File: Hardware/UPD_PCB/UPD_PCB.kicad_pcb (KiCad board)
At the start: 6 copper layers, 145 x 65 mm, 152 parts, among them IC1 STS30-DIS, J1 25A Fuse holder, J10 796739-2, J11 Conn_01x04, J12 Conn_01x02, J2 796739-2, J3 Conn_01x02, J4 1776119-2, J5 1776119-2, J6 1776119-2, J7 1776119-2, J8 1776119-2, J9 1776119-2, Q1 LMR51635XDDCR, Q2 LMR51635XDDCR, Q3 LMR51635XDDCR, Q4 LMR51635XDDCR, Q5 LMR51635XDDCR, Q6 LMR51635XDDCR, Q7 BSS84, U1 ACS711xEXLT-31AB, U2 INA219AxD, U3 INA219AxD, U4 INA219AxD, U5 INA219AxD, U6 INA219AxD, U7 INA219AxD

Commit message: Version 1.1 of PCB
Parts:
- J12: value Conn_01x02 -> Conn_01x01; footprint Connector_PinHeader_1.00mm:PinHeader_1x02_P1.00mm_Vertical -> Connector_PinHeader_2.54mm:PinHeader_1x01_P2.54mm_Vertical
- J3: footprint Connector_PinHeader_1.00mm:PinHeader_1x02_P1.00mm_Vertical -> Connector_JST:JST_EH_B2B-EH-A_1x02_P2.50mm_Vertical
- R13, R26, R27, R36, R37: value 0.2R -> 0.1R
- R14: value 2mR -> 0.1R
- moved J3 1.08 mm to (106.5, 106.0)
- moved J12 0.96 mm to (236.6, 111.2), turned to 0 degrees
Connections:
- J12 pad 1: GND -> VIOUT
- U5 pad 1: INA_SCL -> +5V_out
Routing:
- net +5V_out: track 104.6 -> 107.2 mm
- net INA_SCL: track 200.1 -> 199.2 mm
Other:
- board text added: "5V"
- board text added: "Universal power distribution V1.1"
- board text removed: "Universal power distribution V1.0"

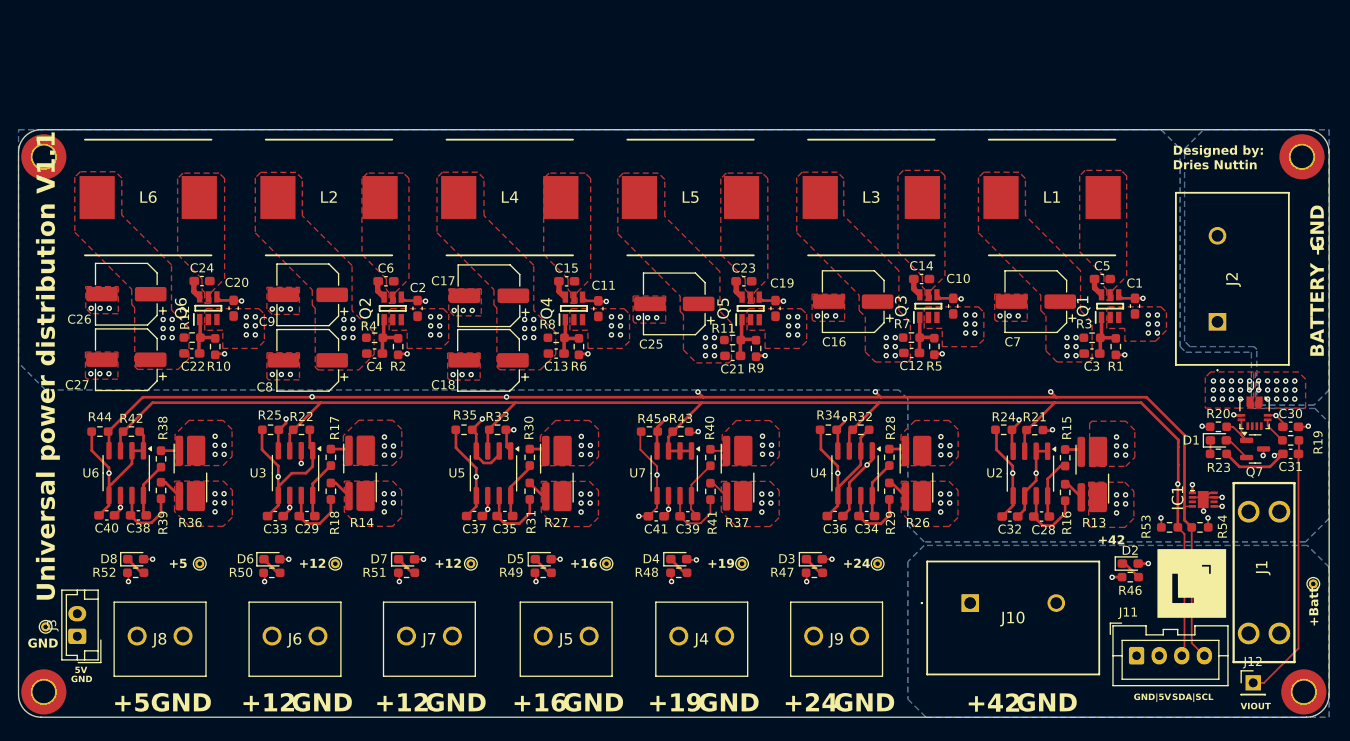
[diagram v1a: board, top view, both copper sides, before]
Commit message: Full system monitoring of PCB
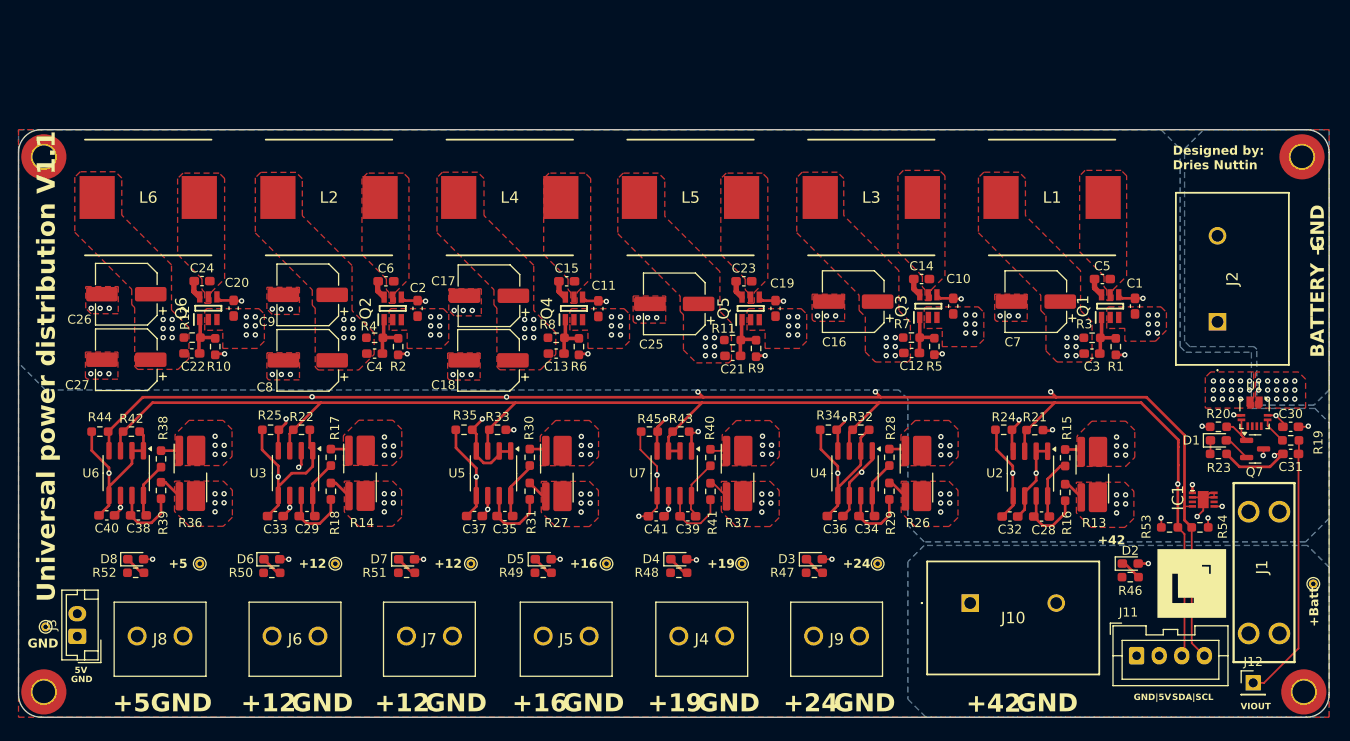
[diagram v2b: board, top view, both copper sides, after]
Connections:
- R13 pad 2: Net-(R13-Pad2) -> +24V
- R13 pad 3: Net-(R13-Pad3) -> +24V_out
- R14 pad 2: Net-(R14-Pad2) -> +12V_1
- R14 pad 3: Net-(R14-Pad3) -> +12V_1_out
- R15 pad 1: Net-(R13-Pad2) -> +24V
- R16 pad 1: Net-(R13-Pad3) -> +24V_out
- R17 pad 1: Net-(R14-Pad2) -> +12V_1
- R18 pad 1: Net-(R14-Pad3) -> +12V_1_out
- R26 pad 2: Net-(R26-Pad2) -> +19V
- R26 pad 3: Net-(R26-Pad3) -> +19V_out
- R27 pad 2: Net-(R27-Pad2) -> +12V_2
- R27 pad 3: Net-(R27-Pad3) -> +12V_2_out
- R28 pad 1: Net-(R26-Pad2) -> +19V
- R29 pad 1: Net-(R26-Pad3) -> +19V_out
- R30 pad 1: Net-(R27-Pad2) -> +12V_2
- R31 pad 1: Net-(R27-Pad3) -> +12V_2_out
- R36 pad 2: Net-(R36-Pad2) -> +5V_NS
- R36 pad 3: Net-(R36-Pad3) -> +5V_out
- R37 pad 2: Net-(R37-Pad2) -> +16V
- R37 pad 3: Net-(R37-Pad3) -> +16V_out
- R38 pad 1: Net-(R36-Pad2) -> +5V_NS
- R39 pad 1: Net-(R36-Pad3) -> +5V_out
- R40 pad 1: Net-(R37-Pad2) -> +16V
- R41 pad 1: Net-(R37-Pad3) -> +16V_out
- U5 pad 1: +5V_out -> INA_SCL
- U7 pad 1: INA_SDA -> +5V_out
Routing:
- net GND: track 76.6 -> 70.0 mm, vias 58 -> 50
- net Net-(R36-Pad3): track 2.67 -> 0.00 mm
- net Net-(R14-Pad3): track 2.61 -> 0.00 mm
- net +12V_1_out: track 1.08 -> 3.68 mm
- net Net-(R27-Pad3): track 2.40 -> 0.00 mm
- net Net-(R26-Pad3): track 2.40 -> 0.00 mm
- net +19V_out: track 1.08 -> 3.47 mm
- net +12V_2_out: track 1.08 -> 3.47 mm
- net Net-(R37-Pad3): track 2.39 -> 0.00 mm
- net +16V_out: track 1.08 -> 3.46 mm
- net Net-(R13-Pad3): track 2.38 -> 0.00 mm
- net +24V_out: track 1.08 -> 3.46 mm
- net +5V_out: track 107.2 -> 109.5 mm
- net Net-(R14-Pad2): track 2.07 -> 0.00 mm
- net +12V_1: track 0.00 -> 2.07 mm
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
